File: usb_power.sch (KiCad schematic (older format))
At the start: 56 parts, among them J1 M20-8770642R, J2 USB_C16PIN, J3 M20-8770642R, Q1 IRLML6402, Q2 BSS214NW, U1 FT230XS, U2 MCP1726-3302ESN, U3 MIC5319-1.8YD5-TR

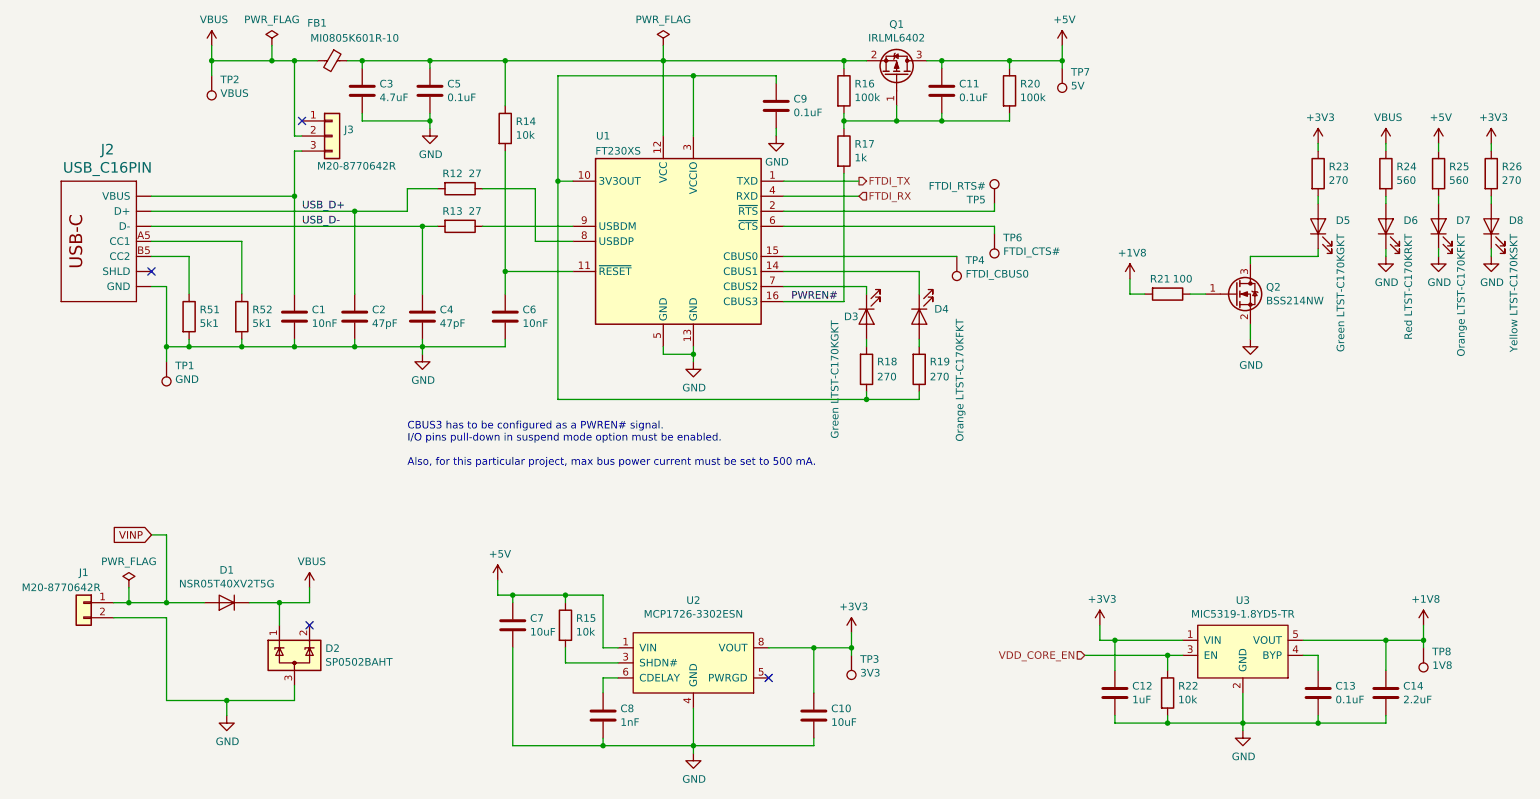
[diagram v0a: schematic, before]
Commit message: Re-annotated all elements
This is a step to prepare for a change from 0805 to 0603 components. Not
critical but nice to have them in order.
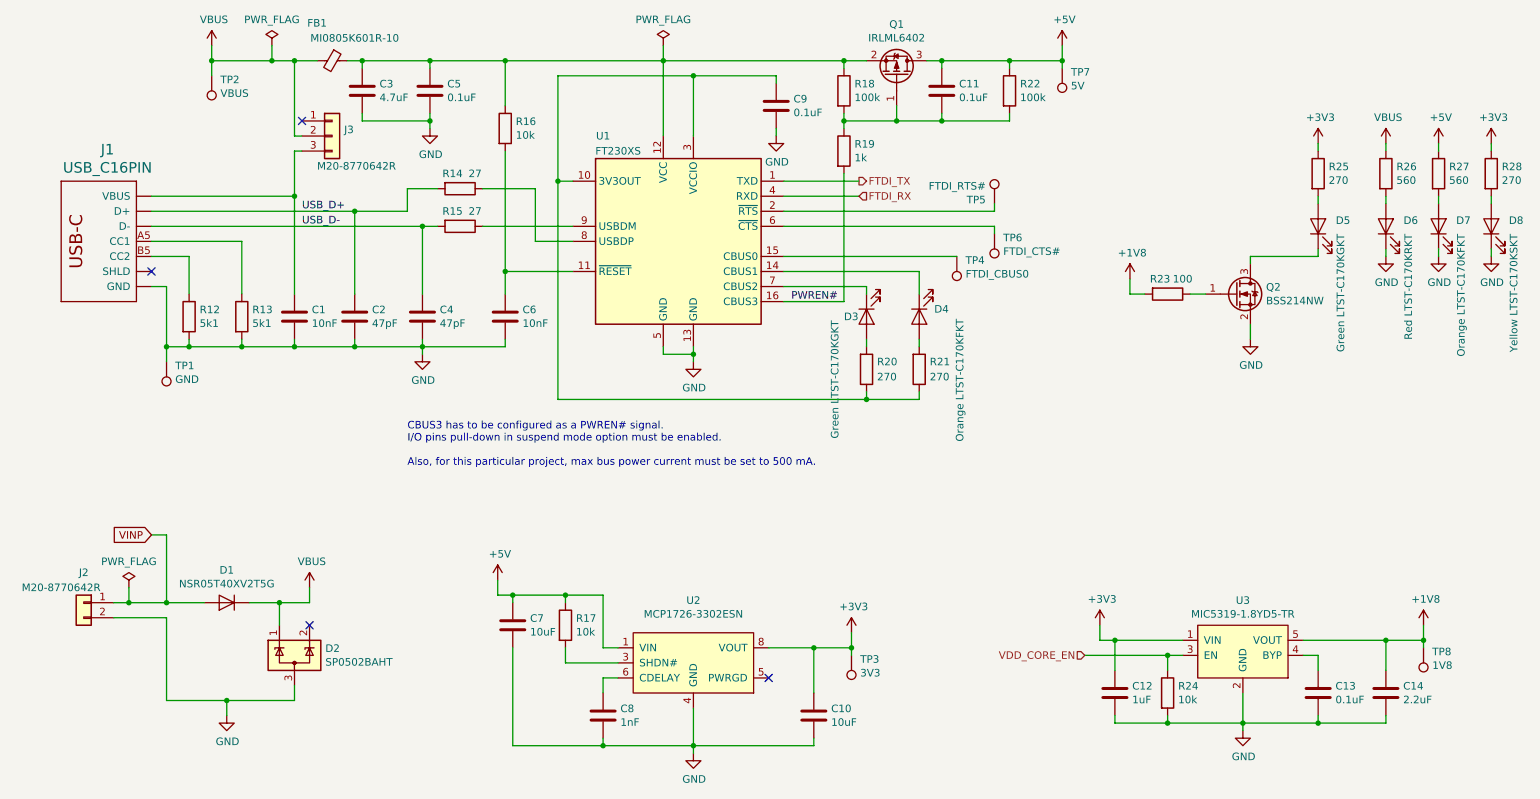
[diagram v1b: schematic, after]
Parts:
- renumbered J2 to J1, J1 to J2, R51 to R12, R52 to R13, R12 to R14, R13 to R15, R14 to R16, R15 to R17, R16 to R18, R17 to R19, R18 to R20, R19 to R21, R20 to R22, R21 to R23, R22 to R24, R23 to R25, R24 to R26, R25 to R27, R26 to R28

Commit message: Use 0603 components, on both sides, route header
This decision was due to the current placement overcrowded and to the
fact that successful routing on one side was uncertain.
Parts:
- C1, C10, C11, C12, C13, C14, C2, C3, C4, C5, C6, C7, C8, C9: footprint Capacitor_SMD:C_0805_2012Metric_Pad1.15x1.40mm_HandSolder -> Capacitor_SMD:C_0603_1608Metric_Pad1.05x0.95mm_HandSolder
- R12, R13, R14, R15, R16, R17, R18, R19, R20, R21, R22, R23, R24, R25, R26, R27, R28: footprint Resistor_SMD:R_0805_2012Metric_Pad1.15x1.40mm_HandSolder -> Resistor_SMD:R_0603_1608Metric_Pad1.05x0.95mm_HandSolder
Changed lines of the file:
@@
 F 0 "R26" H 9620 2146 50  0000 L CNN
 F 1 "560" H 9620 2055 50  0000 L CNN
-F 2 "Resistor_SMD:R_0805_2012Metric_Pad1.15x1.40mm_HandSolder" V 9480 2100 50  0001 C CNN
+F 2 "Resistor_SMD:R_0603_1608Metric_Pad1.05x0.95mm_HandSolder" V 9480 2100 50  0001 C CNN
 F 3 "~" H 9550 2100 50  0001 C CNN
 	1    9550 2100
@@
 F 0 "R27" H 9970 2146 50  0000 L CNN
 F 1 "560" H 9970 2055 50  0000 L CNN
-F 2 "Resistor_SMD:R_0805_2012Metric_Pad1.15x1.40mm_HandSolder" V 9830 2100 50  0001 C CNN
+F 2 "Resistor_SMD:R_0603_1608Metric_Pad1.05x0.95mm_HandSolder" V 9830 2100 50  0001 C CNN
 F 3 "~" H 9900 2100 50  0001 C CNN
 	1    9900 2100
@@
 F 0 "R28" H 10320 2146 50  0000 L CNN
 F 1 "270" H 10320 2055 50  0000 L CNN
-F 2 "Resistor_SMD:R_0805_2012Metric_Pad1.15x1.40mm_HandSolder" V 10180 2100 50  0001 C CNN
+F 2 "Resistor_SMD:R_0603_1608Metric_Pad1.05x0.95mm_HandSolder" V 10180 2100 50  0001 C CNN
 F 3 "~" H 10250 2100 50  0001 C CNN
 	1    10250 2100
@@
 F 0 "C13" H 9215 5596 50  0000 L CNN
 F 1 "0.1uF" H 9215 5505 50  0000 L CNN
-F 2 "Capacitor_SMD:C_0805_2012Metric_Pad1.15x1.40mm_HandSolder" H 9138 5400 50  0001 C CNN
+F 2 "Capacitor_SMD:C_0603_1608Metric_Pad1.05x0.95mm_HandSolder" H 9138 5400 50  0001 C CNN
 F 3 "~" H 9100 5550 50  0001 C CNN
 	1    9100 5550
@@
 F 0 "C14" H 9665 5596 50  0000 L CNN
 F 1 "2.2uF" H 9665 5505 50  0000 L CNN
-F 2 "Capacitor_SMD:C_0805_2012Metric_Pad1.15x1.40mm_HandSolder" H 9588 5400 50  0001 C CNN
+F 2 "Capacitor_SMD:C_0603_1608Metric_Pad1.05x0.95mm_HandSolder" H 9588 5400 50  0001 C CNN
 F 3 "~" H 9550 5550 50  0001 C CNN
 	1    9550 5550
@@
 F 0 "C12" H 7865 5596 50  0000 L CNN
 F 1 "1uF" H 7865 5505 50  0000 L CNN
-F 2 "Capacitor_SMD:C_0805_2012Metric_Pad1.15x1.40mm_HandSolder" H 7788 5400 50  0001 C CNN
+F 2 "Capacitor_SMD:C_0603_1608Metric_Pad1.05x0.95mm_HandSolder" H 7788 5400 50  0001 C CNN
 F 3 "~" H 7750 5550 50  0001 C CNN
 	1    7750 5550
@@
 F 0 "R24" H 8170 5596 50  0000 L CNN
 F 1 "10k" H 8170 5505 50  0000 L CNN
-F 2 "Resistor_SMD:R_0805_2012Metric_Pad1.15x1.40mm_HandSolder" V 8030 5550 50  0001 C CNN
+F 2 "Resistor_SMD:R_0603_1608Metric_Pad1.05x0.95mm_HandSolder" V 8030 5550 50  0001 C CNN
 F 3 "~" H 8100 5550 50  0001 C CNN
 	1    8100 5550
@@
 F 0 "C8" H 4465 5746 50  0000 L CNN
 F 1 "1nF" H 4465 5655 50  0000 L CNN
-F 2 "Capacitor_SMD:C_0805_2012Metric_Pad1.15x1.40mm_HandSolder" H 4388 5550 50  0001 C CNN
+F 2 "Capacitor_SMD:C_0603_1608Metric_Pad1.05x0.95mm_HandSolder" H 4388 5550 50  0001 C CNN
 F 3 "~" H 4350 5700 50  0001 C CNN
 	1    4350 5700
@@
 F 0 "C7" H 3865 5146 50  0000 L CNN
 F 1 "10uF" H 3865 5055 50  0000 L CNN
-F 2 "Capacitor_SMD:C_0805_2012Metric_Pad1.15x1.40mm_HandSolder" H 3788 4950 50  0001 C CNN
+F 2 "Capacitor_SMD:C_0603_1608Metric_Pad1.05x0.95mm_HandSolder" H 3788 4950 50  0001 C CNN
 F 3 "~" H 3750 5100 50  0001 C CNN
 	1    3750 5100
@@
 F 0 "C10" H 5865 5746 50  0000 L CNN
 F 1 "10uF" H 5865 5655 50  0000 L CNN
-F 2 "Capacitor_SMD:C_0805_2012Metric_Pad1.15x1.40mm_HandSolder" H 5788 5550 50  0001 C CNN
+F 2 "Capacitor_SMD:C_0603_1608Metric_Pad1.05x0.95mm_HandSolder" H 5788 5550 50  0001 C CNN
 F 3 "~" H 5750 5700 50  0001 C CNN
 	1    5750 5700
@@
 F 0 "R17" H 4170 5146 50  0000 L CNN
 F 1 "10k" H 4170 5055 50  0000 L CNN
-F 2 "Resistor_SMD:R_0805_2012Metric_Pad1.15x1.40mm_HandSolder" V 4030 5100 50  0001 C CNN
+F 2 "Resistor_SMD:R_0603_1608Metric_Pad1.05x0.95mm_HandSolder" V 4030 5100 50  0001 C CNN
 F 3 "~" H 4100 5100 50  0001 C CNN
 	1    4100 5100
@@
 F 0 "R21" H 6520 3350 50  0000 L CNN
 F 1 "270" H 6520 3450 50  0000 L CNN
-F 2 "Resistor_SMD:R_0805_2012Metric_Pad1.15x1.40mm_HandSolder" V 6380 3400 50  0001 C CNN
+F 2 "Resistor_SMD:R_0603_1608Metric_Pad1.05x0.95mm_HandSolder" V 6380 3400 50  0001 C CNN
 F 3 "~" H 6450 3400 50  0001 C CNN
 	1    6450 3400
@@
 F 0 "R20" H 6170 3350 50  0000 L CNN
 F 1 "270" H 6170 3450 50  0000 L CNN
-F 2 "Resistor_SMD:R_0805_2012Metric_Pad1.15x1.40mm_HandSolder" V 6030 3400 50  0001 C CNN
+F 2 "Resistor_SMD:R_0603_1608Metric_Pad1.05x0.95mm_HandSolder" V 6030 3400 50  0001 C CNN
 F 3 "~" H 6100 3400 50  0001 C CNN
 	1    6100 3400
@@
 F 0 "R19" H 6020 1996 50  0000 L CNN
 F 1 "1k" H 6020 1905 50  0000 L CNN
-F 2 "Resistor_SMD:R_0805_2012Metric_Pad1.15x1.40mm_HandSolder" V 5880 1950 50  0001 C CNN
+F 2 "Resistor_SMD:R_0603_1608Metric_Pad1.05x0.95mm_HandSolder" V 5880 1950 50  0001 C CNN
 F 3 "~" H 5950 1950 50  0001 C CNN
 	1    5950 1950
@@
 F 0 "R14" V 3300 2150 50  0000 C CNN
 F 1 "27" V 3300 2300 50  0000 C CNN
-F 2 "Resistor_SMD:R_0805_2012Metric_Pad1.15x1.40mm_HandSolder" V 3330 2200 50  0001 C CNN
+F 2 "Resistor_SMD:R_0603_1608Metric_Pad1.05x0.95mm_HandSolder" V 3330 2200 50  0001 C CNN
 F 3 "~" H 3400 2200 50  0001 C CNN
 	1    3400 2200
@@
 F 0 "R15" V 3300 2400 50  0000 C CNN
 F 1 "27" V 3300 2550 50  0000 C CNN
-F 2 "Resistor_SMD:R_0805_2012Metric_Pad1.15x1.40mm_HandSolder" V 3330 2450 50  0001 C CNN
+F 2 "Resistor_SMD:R_0603_1608Metric_Pad1.05x0.95mm_HandSolder" V 3330 2450 50  0001 C CNN
 F 3 "~" H 3400 2450 50  0001 C CNN
 	1    3400 2450
@@
 F 0 "C11" H 6715 1596 50  0000 L CNN
 F 1 "0.1uF" H 6715 1505 50  0000 L CNN
-F 2 "Capacitor_SMD:C_0805_2012Metric_Pad1.15x1.40mm_HandSolder" H 6638 1400 50  0001 C CNN
+F 2 "Capacitor_SMD:C_0603_1608Metric_Pad1.05x0.95mm_HandSolder" H 6638 1400 50  0001 C CNN
 F 3 "~" H 6600 1550 50  0001 C CNN
 	1    6600 1550
@@
 F 0 "R18" H 6020 1596 50  0000 L CNN
 F 1 "100k" H 6020 1505 50  0000 L CNN
-F 2 "Resistor_SMD:R_0805_2012Metric_Pad1.15x1.40mm_HandSolder" V 5880 1550 50  0001 C CNN
+F 2 "Resistor_SMD:R_0603_1608Metric_Pad1.05x0.95mm_HandSolder" V 5880 1550 50  0001 C CNN
 F 3 "~" H 5950 1550 50  0001 C CNN
 	1    5950 1550
@@
 F 0 "C1" H 2415 3096 50  0000 L CNN
 F 1 "10nF" H 2415 3005 50  0000 L CNN
-F 2 "Capacitor_SMD:C_0805_2012Metric_Pad1.15x1.40mm_HandSolder" H 2338 2900 50  0001 C CNN
+F 2 "Capacitor_SMD:C_0603_1608Metric_Pad1.05x0.95mm_HandSolder" H 2338 2900 50  0001 C CNN
 F 3 "~" H 2300 3050 50  0001 C CNN
 	1    2300 3050
@@
 F 0 "C4" H 3265 3096 50  0000 L CNN
 F 1 "47pF" H 3265 3005 50  0000 L CNN
-F 2 "Capacitor_SMD:C_0805_2012Metric_Pad1.15x1.40mm_HandSolder" H 3188 2900 50  0001 C CNN
+F 2 "Capacitor_SMD:C_0603_1608Metric_Pad1.05x0.95mm_HandSolder" H 3188 2900 50  0001 C CNN
 F 3 "~" H 3150 3050 50  0001 C CNN
 	1    3150 3050
@@
 F 0 "C2" H 2815 3096 50  0000 L CNN
 F 1 "47pF" H 2815 3005 50  0000 L CNN
-F 2 "Capacitor_SMD:C_0805_2012Metric_Pad1.15x1.40mm_HandSolder" H 2738 2900 50  0001 C CNN
+F 2 "Capacitor_SMD:C_0603_1608Metric_Pad1.05x0.95mm_HandSolder" H 2738 2900 50  0001 C CNN
 F 3 "~" H 2700 3050 50  0001 C CNN
 	1    2700 3050
@@
 F 0 "C6" H 3815 3096 50  0000 L CNN
 F 1 "10nF" H 3815 3005 50  0000 L CNN
-F 2 "Capacitor_SMD:C_0805_2012Metric_Pad1.15x1.40mm_HandSolder" H 3738 2900 50  0001 C CNN
+F 2 "Capacitor_SMD:C_0603_1608Metric_Pad1.05x0.95mm_HandSolder" H 3738 2900 50  0001 C CNN
 F 3 "~" H 3700 3050 50  0001 C CNN
 	1    3700 3050
@@
 F 0 "R16" H 3770 1846 50  0000 L CNN
 F 1 "10k" H 3770 1755 50  0000 L CNN
-F 2 "Resistor_SMD:R_0805_2012Metric_Pad1.15x1.40mm_HandSolder" V 3630 1800 50  0001 C CNN
+F 2 "Resistor_SMD:R_0603_1608Metric_Pad1.05x0.95mm_HandSolder" V 3630 1800 50  0001 C CNN
 F 3 "~" H 3700 1800 50  0001 C CNN
 	1    3700 1800
@@
 F 0 "C9" H 5615 1696 50  0000 L CNN
 F 1 "0.1uF" H 5615 1605 50  0000 L CNN
-F 2 "Capacitor_SMD:C_0805_2012Metric_Pad1.15x1.40mm_HandSolder" H 5538 1500 50  0001 C CNN
+F 2 "Capacitor_SMD:C_0603_1608Metric_Pad1.05x0.95mm_HandSolder" H 5538 1500 50  0001 C CNN
 F 3 "~" H 5500 1650 50  0001 C CNN
 	1    5500 1650
@@
 F 0 "R25" H 9170 2146 50  0000 L CNN
 F 1 "270" H 9170 2055 50  0000 L CNN
-F 2 "Resistor_SMD:R_0805_2012Metric_Pad1.15x1.40mm_HandSolder" V 9030 2100 50  0001 C CNN
+F 2 "Resistor_SMD:R_0603_1608Metric_Pad1.05x0.95mm_HandSolder" V 9030 2100 50  0001 C CNN
 F 3 "~" H 9100 2100 50  0001 C CNN
 	1    9100 2100
@@
 F 0 "R23" V 8000 2850 50  0000 C CNN
 F 1 "100" V 8000 3000 50  0000 C CNN
-F 2 "Resistor_SMD:R_0805_2012Metric_Pad1.15x1.40mm_HandSolder" V 8030 2900 50  0001 C CNN
+F 2 "Resistor_SMD:R_0603_1608Metric_Pad1.05x0.95mm_HandSolder" V 8030 2900 50  0001 C CNN
 F 3 "~" H 8100 2900 50  0001 C CNN
 	1    8100 2900
@@
 F 0 "C5" H 3315 1596 50  0000 L CNN
 F 1 "0.1uF" H 3315 1505 50  0000 L CNN
-F 2 "Capacitor_SMD:C_0805_2012Metric_Pad1.15x1.40mm_HandSolder" H 3238 1400 50  0001 C CNN
+F 2 "Capacitor_SMD:C_0603_1608Metric_Pad1.05x0.95mm_HandSolder" H 3238 1400 50  0001 C CNN
 F 3 "~" H 3200 1550 50  0001 C CNN
 	1    3200 1550
@@
 F 0 "C3" H 2865 1596 50  0000 L CNN
 F 1 "4.7uF" H 2865 1505 50  0000 L CNN
-F 2 "Capacitor_SMD:C_0805_2012Metric_Pad1.15x1.40mm_HandSolder" H 2788 1400 50  0001 C CNN
+F 2 "Capacitor_SMD:C_0603_1608Metric_Pad1.05x0.95mm_HandSolder" H 2788 1400 50  0001 C CNN
 F 3 "~" H 2750 1550 50  0001 C CNN
 	1    2750 1550
@@
 F 0 "R22" H 7120 1596 50  0000 L CNN
 F 1 "100k" H 7120 1505 50  0000 L CNN
-F 2 "Resistor_SMD:R_0805_2012Metric_Pad1.15x1.40mm_HandSolder" V 6980 1550 50  0001 C CNN
+F 2 "Resistor_SMD:R_0603_1608Metric_Pad1.05x0.95mm_HandSolder" V 6980 1550 50  0001 C CNN
 F 3 "~" H 7050 1550 50  0001 C CNN
 	1    7050 1550
@@
 F 0 "R13" H 2020 3096 50  0000 L CNN
 F 1 "5k1" H 2020 3005 50  0000 L CNN
-F 2 "Resistor_SMD:R_0805_2012Metric_Pad1.15x1.40mm_HandSolder" V 1880 3050 50  0001 C CNN
+F 2 "Resistor_SMD:R_0603_1608Metric_Pad1.05x0.95mm_HandSolder" V 1880 3050 50  0001 C CNN
 F 3 "~" H 1950 3050 50  0001 C CNN
 	1    1950 3050
@@
 F 0 "R12" H 1670 3096 50  0000 L CNN
 F 1 "5k1" H 1670 3005 50  0000 L CNN
-F 2 "Resistor_SMD:R_0805_2012Metric_Pad1.15x1.40mm_HandSolder" V 1530 3050 50  0001 C CNN
+F 2 "Resistor_SMD:R_0603_1608Metric_Pad1.05x0.95mm_HandSolder" V 1530 3050 50  0001 C CNN
 F 3 "~" H 1600 3050 50  0001 C CNN
 	1    1600 3050

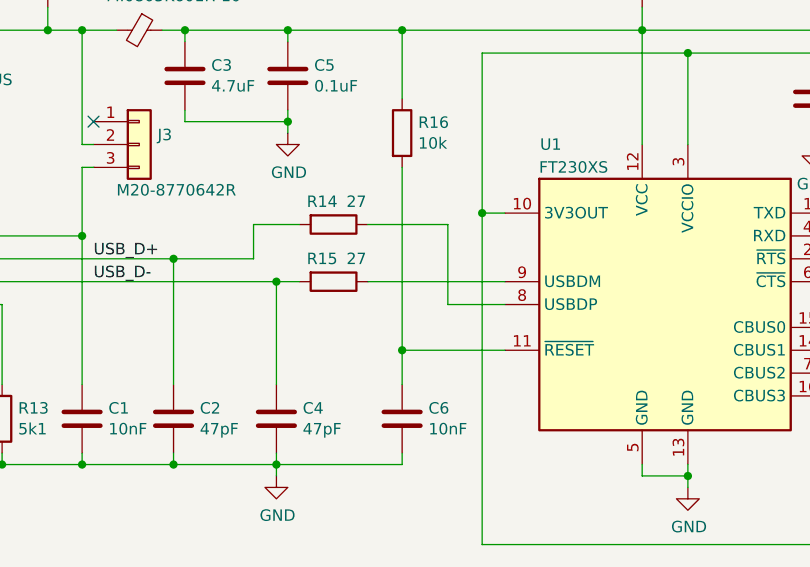
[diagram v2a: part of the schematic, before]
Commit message: FTDI placement proposal, not connected yet
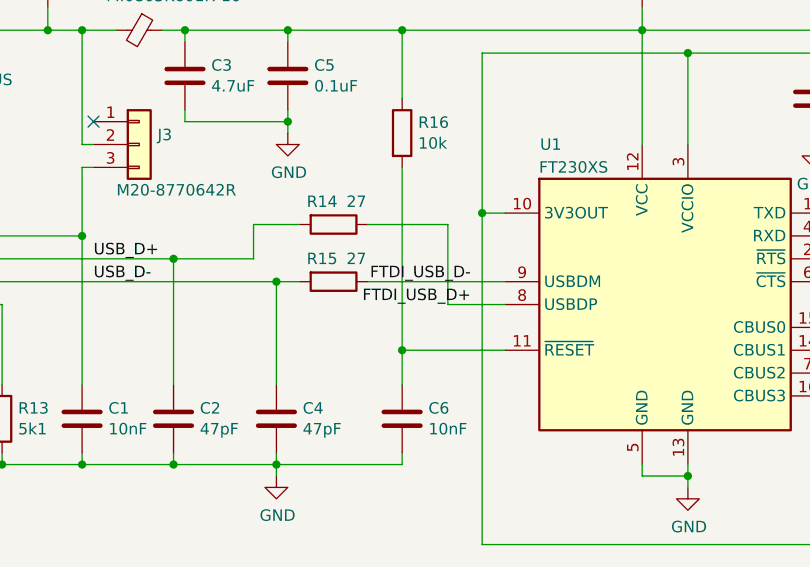
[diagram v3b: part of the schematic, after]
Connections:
- net FTDI_USB_D+: now reaches R14.1, U1.8 (USBDP)
- net FTDI_USB_D-: now reaches R15.1, U1.9 (USBDM)
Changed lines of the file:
@@
 	1450 3350 1450 3250
 Connection ~ 1450 3250
+Text Label 4000 2550 2    50   ~ 0
+FTDI_USB_D+
+Text Label 4000 2450 2    50   ~ 0
+FTDI_USB_D-
 $EndSCHEMATC
